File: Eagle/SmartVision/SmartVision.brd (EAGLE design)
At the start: 30 x 30 mm, 53 parts, among them U1 SMALL_MAVRIC_IMU_MPU-9250, Y1 SMALL_MAVRIC_ABM10

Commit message: Routing mostly complete !
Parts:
- added U$52: CON_2.54MM_16PINS_STACKABLE, STM32F4:CON_2.54MM_16PINS_STACKABLE
- moved U$2 92.7 mm to (-0.91, -10.7), flipped to the bottom, turned to 270 degrees
- moved U$43 86.0 mm to (13.4, -9.23), turned to 90 degrees
- moved U$33 82.6 mm to (-0.93, -5.82), flipped to the bottom
- moved U$42 80.7 mm to (12.4, -5.83)
- moved U$47 80.7 mm to (12.6, -12.3), turned to 180 degrees
- moved U$8 79.9 mm to (0.45, -11.0), turned to 180 degrees
- moved U$7 79.3 mm to (4.96, -10.7), turned to 270 degrees
- moved U$35 78.3 mm to (-5.57, 1.77), flipped to the bottom, turned to 90 degrees
- moved U$21 77.9 mm to (3.69, -5.98), flipped to the bottom
- moved U$22 77.4 mm to (7.63, 9.89), turned to 90 degrees
- moved U$27 77.4 mm to (10.1, -5.30), flipped to the bottom, turned to 180 degrees
- moved U$3 76.7 mm to (0.41, -9.79), turned to 180 degrees
- moved U$44 74.7 mm to (3.87, 6.00), flipped to the bottom
- moved U$46 74.2 mm to (11.4, -9.32), turned to 270 degrees
- moved U$29 74.1 mm to (-11.2, -7.10), flipped to the bottom, turned to 90 degrees
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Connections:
- new net CAN2_RX: U$1.P51, U$52.P15
- new net CAN2_TX: U$1.P52, U$52.P16
- new net UART4_RX: U$1.P24, U$52.P10
- new net UART4_TX: U$1.P23, U$52.P9
- net GND: now also U$52.P1
- net I2C_SCL: now also U$52.P13
- net I2C_SDA: now also U$52.P14
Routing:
- net N$17: track 0.00 -> 14.3 mm, vias 0 -> 2
- net N$18: track 0.00 -> 11.8 mm, vias 0 -> 1
- net N$20: track 0.00 -> 11.6 mm, vias 0 -> 2
- net N$14: track 0.00 -> 9.43 mm
- net N$13: track 0.00 -> 9.39 mm, vias 0 -> 3
- net I2C_SDA: track 0.00 -> 8.96 mm
- net GND: track 0.00 -> 8.80 mm
- net VCC: track 0.00 -> 8.80 mm
- net USB_D-: track 0.00 -> 7.45 mm, vias 0 -> 2
- net USB_D+: track 0.00 -> 7.30 mm, vias 0 -> 2
- net VCC_ANA: track 0.00 -> 6.93 mm
- net N$19: track 0.00 -> 6.66 mm, vias 0 -> 1
- net N$8: track 0.00 -> 6.38 mm, vias 0 -> 1
- net I2C_SCL: track 0.00 -> 5.77 mm, vias 0 -> 1
- net USB_ID: track 0.00 -> 5.65 mm
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
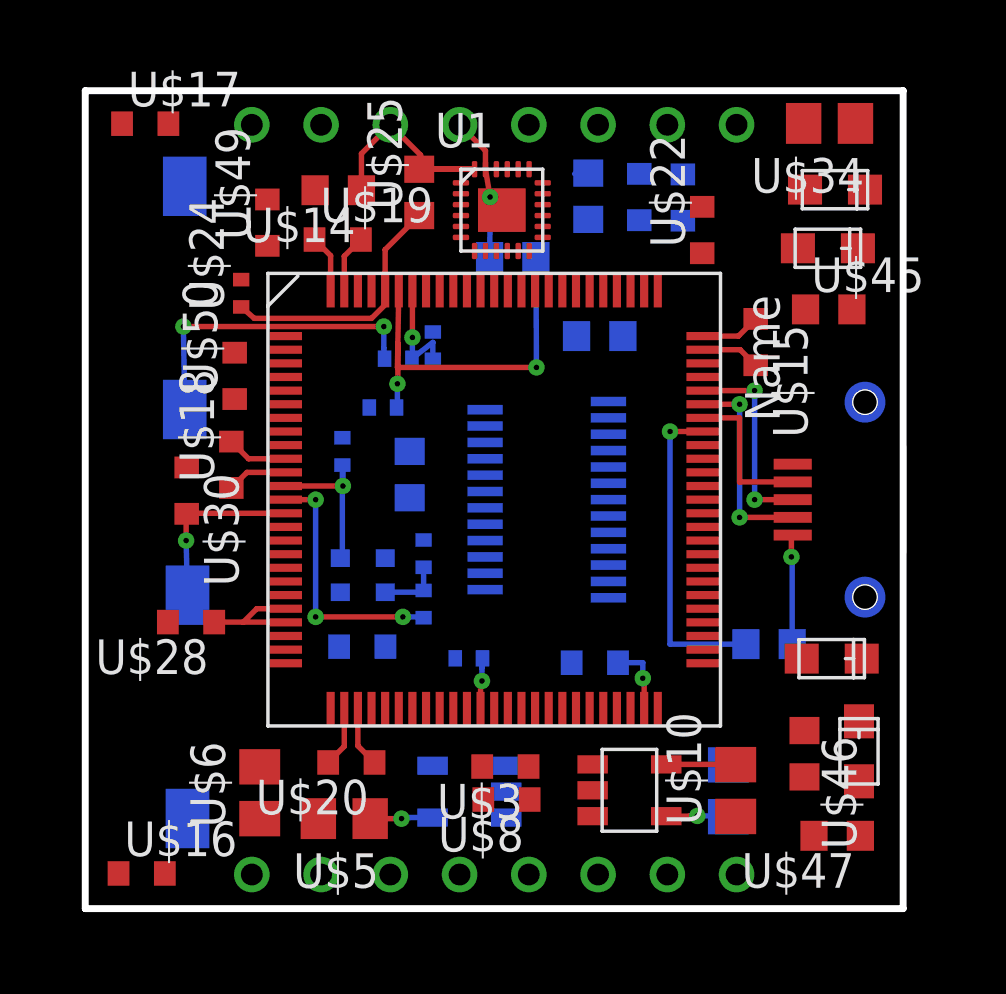
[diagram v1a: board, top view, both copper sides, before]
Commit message: Routing finish
Routing without autorouter.
Need optimisation, symbol, value, …
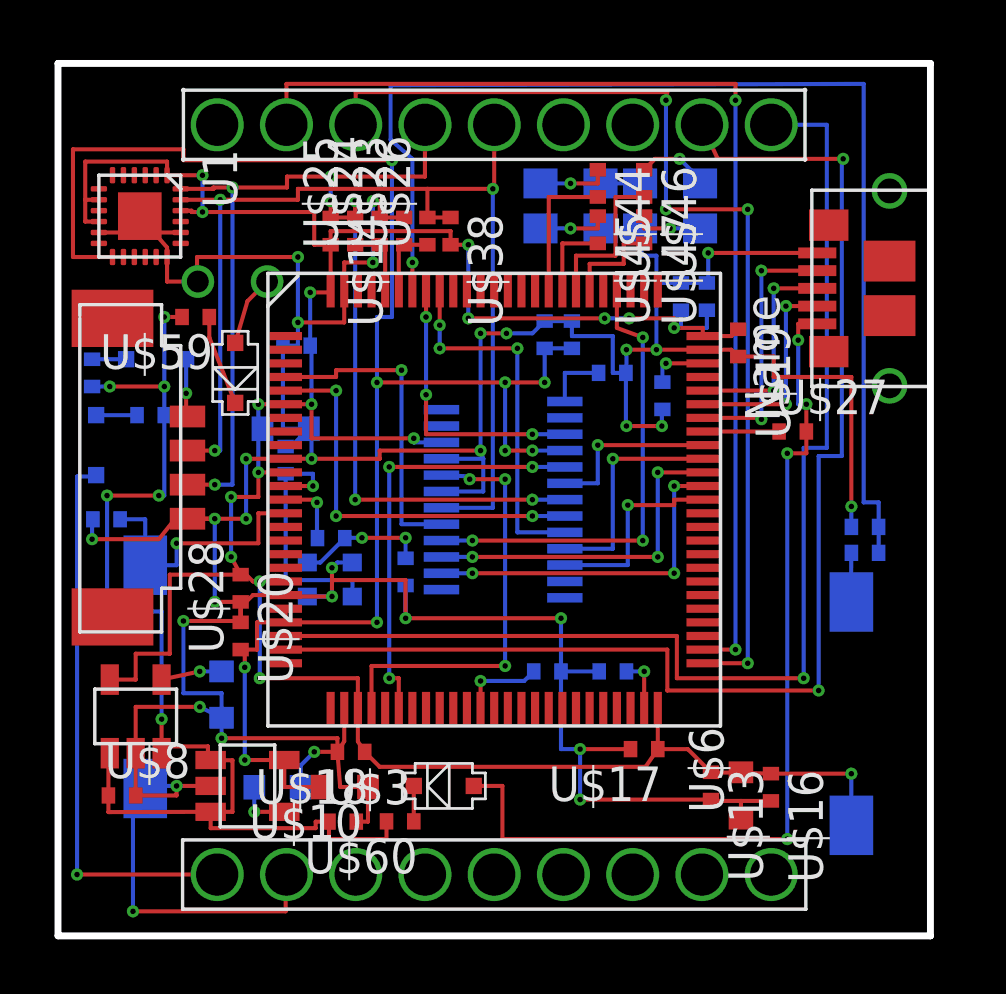
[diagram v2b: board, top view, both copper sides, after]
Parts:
- added U$53: CON_1.25MM_4PINS, STM32F4:CON_1.25MM_4PINS
- added U$54: CON_2.54MM_2PINS_STACKABLE, STM32F4:CON_2.54MM_2PINS_STACKABLE
- added U$55, U$56, U$57, U$61: DIODE_SCHOTTKY, STM32F4:DIODE_SCHOTTKY
- added U$58, U$59, U$62: 28, small_mavric:SMALL_MAVRIC_SMALL_MAVRIC_RESISTOR_R0402
- added U$60: 12.5, small_mavric:SMALL_MAVRIC_SMALL_MAVRIC_RESISTOR_R0402
- U$10, U$34, U$5, U$6, U$9: device small_mavric:SMALL_MAVRIC_SMALL_MAVRIC_CAPACITOR_C0805 -> small_mavric:SMALL_MAVRIC_SMALL_MAVRIC_CAPACITOR_C0603
- U$12, U$14, U$25, U$26, U$27, U$38: device small_mavric:SMALL_MAVRIC_SMALL_MAVRIC_RESISTOR_R0603 -> small_mavric:SMALL_MAVRIC_SMALL_MAVRIC_RESISTOR_R0402
- U$13, U$15, U$16, U$17, U$18, U$19, U$20, U$21, U$22, U$28, U$3, U$30, U$39, U$48, U$49, U$50, U$8: device small_mavric:SMALL_MAVRIC_SMALL_MAVRIC_CAPACITOR_C0603 -> small_mavric:SMALL_MAVRIC_SMALL_MAVRIC_CAPACITOR_C0402
- U$44, U$45, U$46, U$47: value 100 -> 402; device small_mavric:SMALL_MAVRIC_SMALL_MAVRIC_RESISTOR_R0603 -> small_mavric:SMALL_MAVRIC_SMALL_MAVRIC_RESISTOR_R0402
- U$52: value CON_2.54MM_16PINS_STACKABLE -> CON_2.54MM_18PINS_STACKABLE; device STM32F4:CON_2.54MM_16PINS_STACKABLE -> STM32F4:CON_2.54MM_18PINS_STACKABLE
- moved U$17 29.3 mm to (5.50, -9.15), turned to 180 degrees
- moved U$31 28.3 mm to (13.1, -7.35), turned to 90 degrees
- moved U$47 23.3 mm to (5.50, 9.90), turned to 270 degrees
- moved U$16 23.3 mm to (10.2, -10.6), turned to 270 degrees
- moved U$34 22.9 mm to (-7.65, 2.60), flipped to the bottom
- moved U$46 21.7 mm to (5.50, 11.6)
- moved U$43 20.4 mm to (6.45, 9.95), flipped to the bottom, turned to 0 degrees
- moved U$32 18.5 mm to (13.6, -1.95)
- moved U$42 18.4 mm to (6.45, 11.6), flipped to the bottom
- moved U$6 17.7 mm to (9.05, -10.8)
- moved U$50 17.6 mm to (7.80, 7.45), flipped to the bottom
- moved U$51 17.2 mm to (13.6, -1.00), turned to 180 degrees
- moved U$15 16.8 mm to (-7.25, 5.65), flipped to the bottom, turned to 0 degrees
- moved U$9 16.5 mm to (-7.95, -10.6), turned to 180 degrees
- moved U$49 15.4 mm to (6.85, 7.45), flipped to the bottom
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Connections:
- new net N$24: U$61.P2, U$62.1
- new net N$27: U$55.P2, U$58.1
- new net N$28: U$56.P2, U$59.1
- new net N$29: U$57.P2, U$60.1
- new net VBAT_C: U$53.P1, U$55.P1
- new net VBAT_P: U$54.P1, U$56.P1
- new net VBAT_S: U$52.P1, U$61.P1
- net CAN2_RX: now also U$52.P16; no longer U$52.P15
- net CAN2_TX: now also U$52.P17; no longer U$52.P16
- net GND: now also U$52.P2, U$53.P4, U$54.P2; no longer U$52.P1
- net I2C_SCL: now also U$52.P14, U$53.P2; no longer U$52.P13
- net I2C_SDA: now also U$52.P15, U$53.P3; no longer U$52.P14
- net UART4_RX: now also U$52.P11; no longer U$52.P10
- net UART4_TX: now also U$52.P10; no longer U$52.P9
- net USB_VBUS: now also U$57.P1
- net VBAT: now also U$58.2, U$59.2, U$60.2, U$62.2
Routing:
- net GND: track 8.80 -> 186.7 mm, vias 0 -> 31
- net VCC: track 8.80 -> 104.4 mm, vias 0 -> 17
- net VCC_ANA: track 6.93 -> 62.4 mm, vias 0 -> 9
- net UART4_RX: track 0.00 -> 47.4 mm, vias 0 -> 2
- net VBAT: track 0.00 -> 44.5 mm, vias 0 -> 6
- net UART4_TX: track 0.00 -> 43.7 mm, vias 0 -> 1
- net CAN2_TX: track 0.00 -> 39.9 mm, vias 0 -> 2
- net N$21: track 4.10 -> 43.0 mm
- net CAN2_RX: track 0.00 -> 38.2 mm, vias 0 -> 4
- net I2C_SDA: track 8.96 -> 45.5 mm, vias 0 -> 7
- net I2C_SCL: track 5.77 -> 40.1 mm, vias 1 -> 3
- net USB_VBUS: track 4.08 -> 34.0 mm, vias 1 -> 4
- net VBAT_S: track 0.00 -> 20.5 mm, vias 0 -> 1
- net D4: track 0.00 -> 17.2 mm, vias 0 -> 3
- net HSYNC: track 0.00 -> 15.8 mm, vias 0 -> 3
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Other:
- board size 30 x 30 mm -> 32 x 32 mm

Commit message: PCB ready for production
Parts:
- removed U$12: 10K, small_mavric:SMALL_MAVRIC_SMALL_MAVRIC_RESISTOR_R0402
- removed U$13, U$15, U$16: 100nF, small_mavric:SMALL_MAVRIC_SMALL_MAVRIC_CAPACITOR_C0402
- removed U$22: 2.2uF, small_mavric:SMALL_MAVRIC_SMALL_MAVRIC_CAPACITOR_C0402
- removed U$27: 4.7K, small_mavric:SMALL_MAVRIC_SMALL_MAVRIC_RESISTOR_R0402
- removed U$32, U$51: 1K, small_mavric:SMALL_MAVRIC_SMALL_MAVRIC_RESISTOR_R0402
- removed U$56: DIODE_SCHOTTKY, STM32F4:DIODE_SCHOTTKY
- removed U$58, U$62: 28, small_mavric:SMALL_MAVRIC_SMALL_MAVRIC_RESISTOR_R0402
- removed U$6: 4.7uF, small_mavric:SMALL_MAVRIC_SMALL_MAVRIC_CAPACITOR_C0603
- added C10: 2.2uF, small_mavric:SMALL_MAVRIC_SMALL_MAVRIC_CAPACITOR_C0402
- added C17: 4.7uF, small_mavric:SMALL_MAVRIC_SMALL_MAVRIC_CAPACITOR_C0603
- added C22, C5, C6: 100nF, small_mavric:SMALL_MAVRIC_SMALL_MAVRIC_CAPACITOR_C0402
- added R1, R2: 1K, small_mavric:SMALL_MAVRIC_SMALL_MAVRIC_RESISTOR_R0402
- added R12, R13: 28, small_mavric:SMALL_MAVRIC_SMALL_MAVRIC_RESISTOR_R0402
- added R15: 12.5, small_mavric:SMALL_MAVRIC_SMALL_MAVRIC_RESISTOR_R0402
- added R17: 10K, small_mavric:SMALL_MAVRIC_SMALL_MAVRIC_RESISTOR_R0402
- added R4: 4.7K, small_mavric:SMALL_MAVRIC_SMALL_MAVRIC_RESISTOR_R0402
- added U$63, U$64: PAD_FLASH, STM32F4:PAD_FLASH
- U$54: value CON_2.54MM_2PINS_STACKABLE -> DIODE_SCHOTTKY; device STM32F4:CON_2.54MM_2PINS_STACKABLE -> STM32F4:DIODE_SCHOTTKY
- U$59: value 28 -> CON_2.54MM_2PINS; device small_mavric:SMALL_MAVRIC_SMALL_MAVRIC_RESISTOR_R0402 -> STM32F4:CON_2.54MM_2PINS
- moved U$31 30.5 mm to (-12.2, 9.75)
- moved U$59 30.0 mm to (13.9, -10.2), turned to 270 degrees
- moved U$54 27.3 mm to (13.9, -5.80), turned to 90 degrees
- moved U$55 1.65 mm to (-12.8, 3.55)
- moved U$61 1.06 mm to (-13.9, 1.20), turned to 180 degrees
- renumbered U$10 to C20, U$14 to R18, U$17 to C4, U$18 to C3, U$19 to C2, U$20 to C1, U$21 to C9, U$23 to C14, U$24 to C15, U$25 to R7, U$26 to R6, U$28 to C7, U$3 to C16, U$30 to C11, U$33 to R5, U$34 to C8, U$35 to C13, U$36 to C12, U$37 to R3, U$38 to R16, U$39 to C23, U$44 to R8, U$45 to R9, U$46 to R10, U$47 to R11, U$48 to C24, U$49 to C25, U$5 to C18, U$50 to C26, U$60 to R14, U$8 to C19, U$9 to C21
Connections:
- removed net N$28: U$56.P2, U$59.1
- new net N$25: R15.1, U$54.P2
- new net SWCLK: U$1.P76, U$63.P$1
- new net SWDIO: U$1.P72, U$64.P$1
- net GND: now also C10.2, C17.1, C22.2, C5.2, C6.2, R17.1, R2.1, U$59.P2; no longer U$12.1, U$13.2, U$15.2, U$16.2, U$22.2, U$51.1, U$54.P2, U$6.1
- net N$16: now also C10.1; no longer U$22.1
- net N$18: now also R4.1; no longer U$27.1
- net N$20: now also R1.1; no longer U$32.1
- net N$21: now also R1.2, R2.2; no longer U$32.2, U$51.2
- net N$24: now also R13.1; no longer U$62.1
- net N$27: now also R12.1; no longer U$58.1
- net N$3: now also R17.2; no longer U$12.2
- net USB_VBUS: now also R4.2; no longer U$27.2
- net VBAT: now also R12.2, R13.2, R15.2; no longer U$58.2, U$59.2, U$62.2
- net VBAT_P: now also U$59.P1; no longer U$56.P1
- net VCC: now also C17.2, C22.1, C5.1, C6.1; no longer U$13.1, U$15.1, U$16.1, U$6.2
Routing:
- net N$21: track 43.0 -> 11.2 mm, vias 1 -> 2
- net VBAT: track 44.5 -> 63.5 mm, vias 6 -> 4
- net CAN2_TX: track 39.9 -> 49.8 mm
- net CAN2_RX: track 38.2 -> 46.5 mm, vias 4 -> 2
- net GND: track 186.7 -> 180.1 mm, vias 31 -> 35
- net N$20: track 1.81 -> 6.75 mm, vias 0 -> 1
- net N$28: track 3.33 -> 0.00 mm
- net SWCLK: track 0.00 -> 3.23 mm
- net SWDIO: track 0.00 -> 2.70 mm
- net N$25: track 0.00 -> 2.50 mm, vias 0 -> 1
- net N$18: track 2.80 -> 4.75 mm
- net VCC: track 104.4 -> 103.6 mm
- net VBAT_P: track 2.61 -> 1.98 mm
- net N$24: track 1.50 -> 0.90 mm
- net D1: track 12.8 -> 13.4 mm
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- added copper zone on layer 1, net GND
- added copper zone on layer 16, net GND
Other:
- board text added: "BOOT1"
- board text added: "NRST"
- board text added: "SMARTVISION V1 EPFL LIS WILLIAM PONSOT"

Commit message: PCB finish with BOM
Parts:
- added U$3, U$5: PAD_FLASH, STM32F4:PAD_FLASH
- moved U$63 8.49 mm to (14.3, 0.70)
- moved U$64 6.86 mm to (14.3, -0.50)
- moved C10 0.75 mm to (6.05, 4.40), turned to 180 degrees
- moved R17 0.30 mm to (4.05, 4.65)
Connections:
- net GND: now also U$3.P$1
- net VBAT: now also U$5.P$1
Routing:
- net SWCLK: track 3.23 -> 14.4 mm
- net SWDIO: track 2.70 -> 10.9 mm
- net VBAT: track 63.5 -> 67.6 mm, vias 4 -> 5
- net GND: track 180.1 -> 176.9 mm, vias 35 -> 33
- net N$16: track 2.29 -> 2.88 mm
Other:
- board text added: "3V"
- board text added: "MOLEX CONNECTOR"
- board text added: "SWCLK"
- board text added: "SWDIO"
- board text added: "USB"
- board text added: "VBAT"
